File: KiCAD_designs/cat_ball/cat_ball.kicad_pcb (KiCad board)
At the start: 2 copper layers, 35 x 34.7 mm, 35 parts, among them J1 B2B-PH-SM4-TBLFSN, J2 B2B-PH-SM4-TBLFSN, U1 ATMEGA328P-AU, U2 MX1508

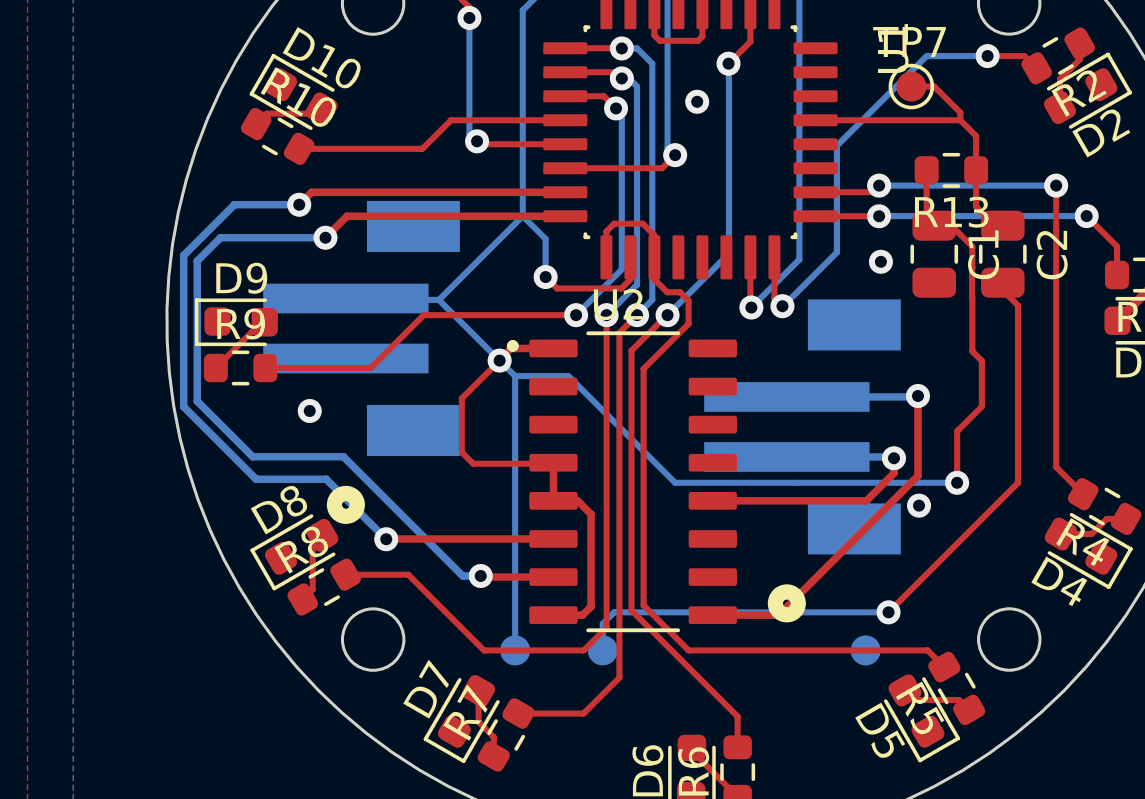
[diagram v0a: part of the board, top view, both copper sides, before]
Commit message: changed cat ball via size
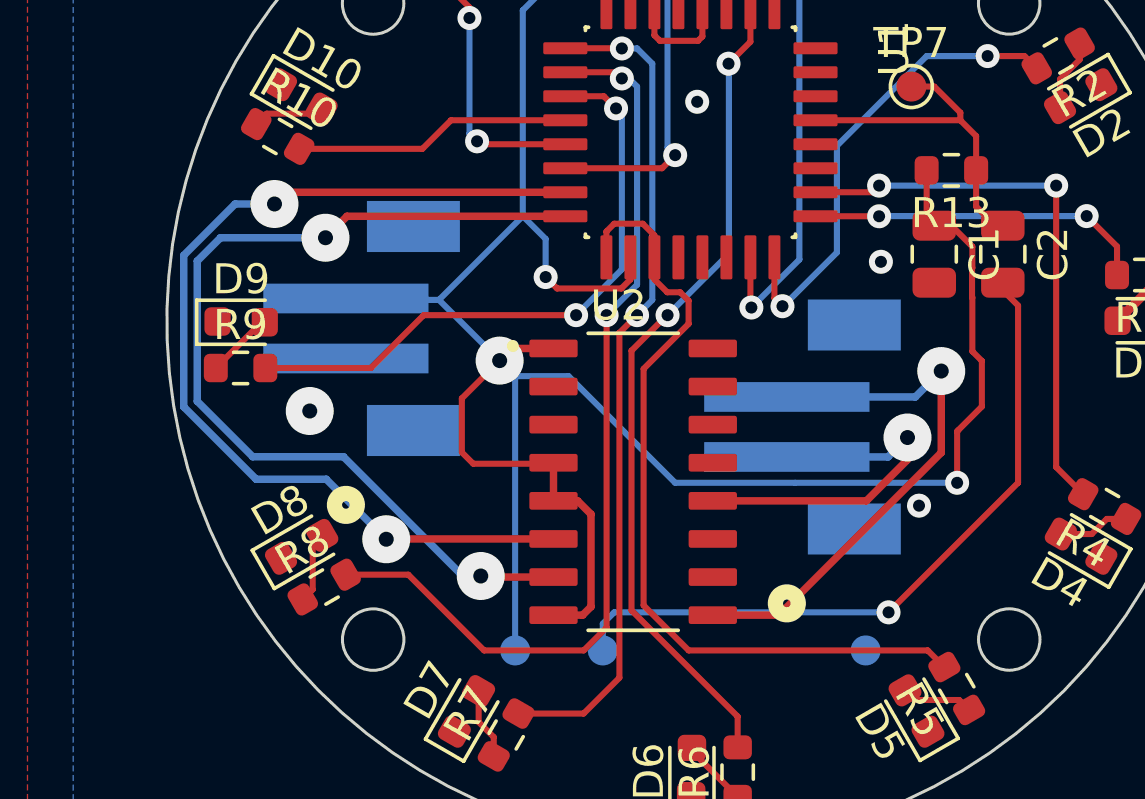
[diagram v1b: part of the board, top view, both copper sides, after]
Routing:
- net Net-(U2A-OUTB2): track 15.8 -> 18.1 mm
- net Net-(U2A-OUTA2): track 10.5 -> 12.1 mm
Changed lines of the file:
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@@
   (via (at 136.8 63.796) (size 0.8) (drill 0.4) (layers "F.Cu" "B.Cu") (net 1))
   (via (at 149.754 81.068) (size 0.8) (drill 0.4) (layers "F.Cu" "B.Cu") (net 1))
-  (via (at 134.505 76.995) (size 0.8) (drill 0.4) (layers "F.Cu" "B.Cu") (net 1))
+  (via (at 134.505 76.995) (size 1.6) (drill 0.5) (layers "F.Cu" "B.Cu") (net 1))
   (via (at 136.038 74.21) (size 0.8) (drill 0.4) (layers "F.Cu" "B.Cu") (net 1))
   (segment (start 136.038 74.21) (end 136.038 72.94) (width 0.2032) (layer "B.Cu") (net 1))
@@
   (via (at 147.214 73.702) (size 0.8) (drill 0.4) (layers "F.Cu" "B.Cu") (free) (net 2))
   (via (at 141.0896 68.368) (size 0.8) (drill 0.4) (layers "F.Cu" "B.Cu") (free) (net 2))
-  (via (at 128.175 78.675) (size 0.8) (drill 0.4) (layers "F.Cu" "B.Cu") (free) (net 2))
+  (via (at 128.175 78.675) (size 1.6) (drill 0.5) (layers "F.Cu" "B.Cu") (free) (net 2))
   (segment (start 150.388 70.654) (end 150.388 71.862) (width 0.2032) (layer "F.Cu") (net 3))
   (segment (start 145.034 68.984) (end 149.862 68.984) (width 0.2032) (layer "F.Cu") (net 3))
@@
   (segment (start 140.102 69.892) (end 140.102 63.796) (width 0.2032) (layer "B.Cu") (net 28))
   (segment (start 140.356 70.146) (end 140.102 69.892) (width 0.2032) (layer "B.Cu") (net 28))
-  (segment (start 136.694 71.384) (end 128.241 71.384) (width 0.25) (layer "F.Cu") (net 35))
+  (segment (start 127 71.775) (end 127.391 71.384) (width 0.25) (layer "F.Cu") (net 35))
   (segment (start 136.3 82.94) (end 130.735 82.94) (width 0.25) (layer "F.Cu") (net 35))
-  (segment (start 128.241 71.384) (end 127.825 71.8) (width 0.25) (layer "F.Cu") (net 35))
   (segment (start 130.735 82.94) (end 130.725 82.95) (width 0.25) (layer "F.Cu") (net 35))
-  (via (at 127.825 71.8) (size 0.8) (drill 0.4) (layers "F.Cu" "B.Cu") (net 35))
-  (via (at 130.725 82.95) (size 0.8) (drill 0.4) (layers "F.Cu" "B.Cu") (net 35))
-  (segment (start 130.725 82.95) (end 128.725 80.95) (width 0.25) (layer "B.Cu") (net 35))
-  (segment (start 125.663604 71.8) (end 127.825 71.8) (width 0.25) (layer "B.Cu") (net 35))
-  (segment (start 123.975 78.536396) (end 123.975 73.488604) (width 0.25) (layer "B.Cu") (net 35))
-  (segment (start 128.725 80.95) (end 126.388604 80.95) (width 0.25) (layer "B.Cu") (net 35))
-  (segment (start 126.388604 80.95) (end 123.975 78.536396) (width 0.25) (layer "B.Cu") (net 35))
-  (segment (start 123.975 73.488604) (end 125.663604 71.8) (width 0.25) (layer "B.Cu") (net 35))
+  (segment (start 127.391 71.384) (end 136.694 71.384) (width 0.25) (layer "F.Cu") (net 35))
+  (via (at 127 71.775) (size 1.6) (drill 0.5) (layers "F.Cu" "B.Cu") (net 35))
+  (via (at 130.725 82.95) (size 1.6) (drill 0.5) (layers "F.Cu" "B.Cu") (net 35))
+  (segment (start 123.975 73.488604) (end 123.975 78.536396) (width 0.25) (layer "B.Cu") (net 35))
+  (segment (start 123.975 78.536396) (end 126.388604 80.95) (width 0.25) (layer "B.Cu") (net 35))
+  (segment (start 126.388604 80.95) (end 128.725 80.95) (width 0.25) (layer "B.Cu") (net 35))
+  (segment (start 128.725 80.95) (end 130.725 82.95) (width 0.25) (layer "B.Cu") (net 35))
+  (segment (start 125.688604 71.775) (end 123.975 73.488604) (width 0.25) (layer "B.Cu") (net 35))
+  (segment (start 127 71.775) (end 125.688604 71.775) (width 0.25) (layer "B.Cu") (net 35))
   (segment (start 136.694 72.184) (end 129.416 72.184) (width 0.25) (layer "F.Cu") (net 36))
   (segment (start 129.416 72.184) (end 128.7 72.9) (width 0.25) (layer "F.Cu") (net 36))
   (segment (start 133.91 84.21) (end 133.875 84.175) (width 0.25) (layer "F.Cu") (net 36))
   (segment (start 136.3 84.21) (end 133.91 84.21) (width 0.25) (layer "F.Cu") (net 36))
-  (via (at 128.7 72.9) (size 0.8) (drill 0.4) (layers "F.Cu" "B.Cu") (net 36))
-  (via (at 133.875 84.175) (size 0.8) (drill 0.4) (layers "F.Cu" "B.Cu") (net 36))
+  (via (at 128.7 72.9) (size 1.6) (drill 0.5) (layers "F.Cu" "B.Cu") (net 36))
+  (via (at 133.875 84.175) (size 1.6) (drill 0.5) (layers "F.Cu" "B.Cu") (net 36))
   (segment (start 124.425 78.35) (end 124.425 73.675) (width 0.25) (layer "B.Cu") (net 36))
   (segment (start 126.275 80.2) (end 124.425 78.35) (width 0.25) (layer "B.Cu") (net 36))
@@
   (segment (start 124.425 73.675) (end 125.2 72.9) (width 0.25) (layer "B.Cu") (net 36))
   (segment (start 133.875 84.175) (end 133.275 84.175) (width 0.25) (layer "B.Cu") (net 36))
-  (segment (start 141.61 81.67) (end 146.73 81.67) (width 0.25) (layer "F.Cu") (net 41))
-  (segment (start 146.73 81.67) (end 147.65 80.75) (width 0.25) (layer "F.Cu") (net 41))
-  (segment (start 147.65 80.75) (end 147.65 80.25) (width 0.25) (layer "F.Cu") (net 41))
-  (via (at 147.65 80.25) (size 0.8) (drill 0.4) (layers "F.Cu" "B.Cu") (net 41))
-  (segment (start 147.60725 80.20725) (end 144.077949 80.20725) (width 0.25) (layer "B.Cu") (net 41))
-  (segment (start 147.65 80.25) (end 147.60725 80.20725) (width 0.25) (layer "B.Cu") (net 41))
+  (segment (start 148.1 80.3) (end 146.73 81.67) (width 0.25) (layer "F.Cu") (net 41))
+  (segment (start 146.73 81.67) (end 141.61 81.67) (width 0.25) (layer "F.Cu") (net 41))
+  (segment (start 148.1 79.558852) (end 148.1 80.3) (width 0.25) (layer "F.Cu") (net 41))
+  (via (at 148.1 79.558852) (size 1.6) (drill 0.5) (layers "F.Cu" "B.Cu") (net 41))
+  (segment (start 147.451602 80.20725) (end 144.077949 80.20725) (width 0.25) (layer "B.Cu") (net 41))
+  (segment (start 148.1 79.558852) (end 147.451602 80.20725) (width 0.25) (layer "B.Cu") (net 41))
+  (segment (start 149.225 77.343) (end 149.225 80.063695) (width 0.25) (layer "F.Cu") (net 42))
+  (segment (start 149.225 80.063695) (end 143.808695 85.48) (width 0.25) (layer "F.Cu") (net 42))
   (segment (start 143.808695 85.48) (end 141.61 85.48) (width 0.25) (layer "F.Cu") (net 42))
-  (segment (start 148.45 78.175) (end 148.45 80.838695) (width 0.25) (layer "F.Cu") (net 42))
-  (segment (start 148.45 80.838695) (end 143.808695 85.48) (width 0.25) (layer "F.Cu") (net 42))
-  (via (at 148.45 78.175) (size 0.8) (drill 0.4) (layers "F.Cu" "B.Cu") (net 42))
-  (segment (start 148.417752 78.207248) (end 148.45 78.175) (width 0.25) (layer "B.Cu") (net 42))
-  (segment (start 144.077949 78.207248) (end 148.417752 78.207248) (width 0.25) (layer "B.Cu") (net 42))
+  (via (at 149.225 77.343) (size 1.6) (drill 0.5) (layers "F.Cu" "B.Cu") (net 42))
+  (segment (start 149.225 77.343) (end 148.360752 78.207248) (width 0.25) (layer "B.Cu") (net 42))
+  (segment (start 148.360752 78.207248) (end 144.077949 78.207248) (width 0.25) (layer "B.Cu") (net 42))
   (zone (net 2) (net_name "GND") (layer "F.Cu") (hatch edge 0.5)
     (connect_pads (clearance 0.2))

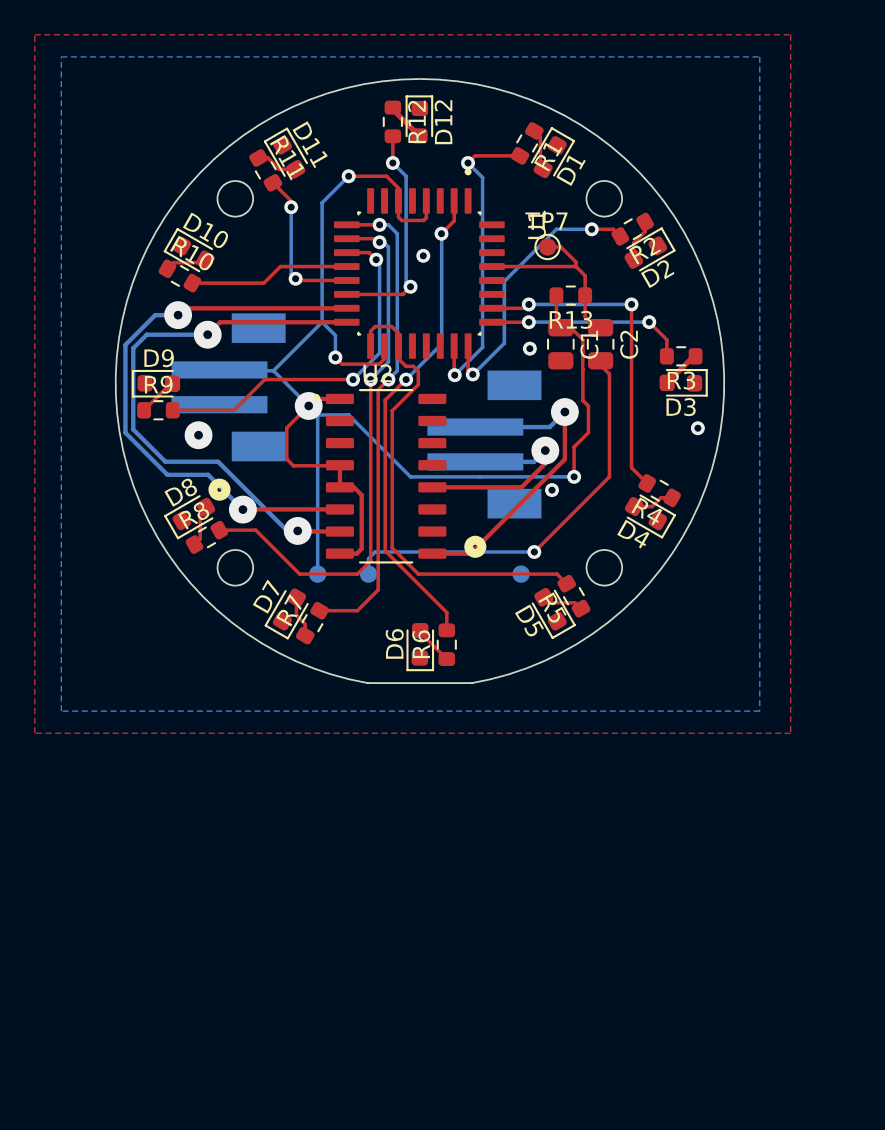
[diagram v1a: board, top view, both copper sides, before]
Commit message: catball thicker traces
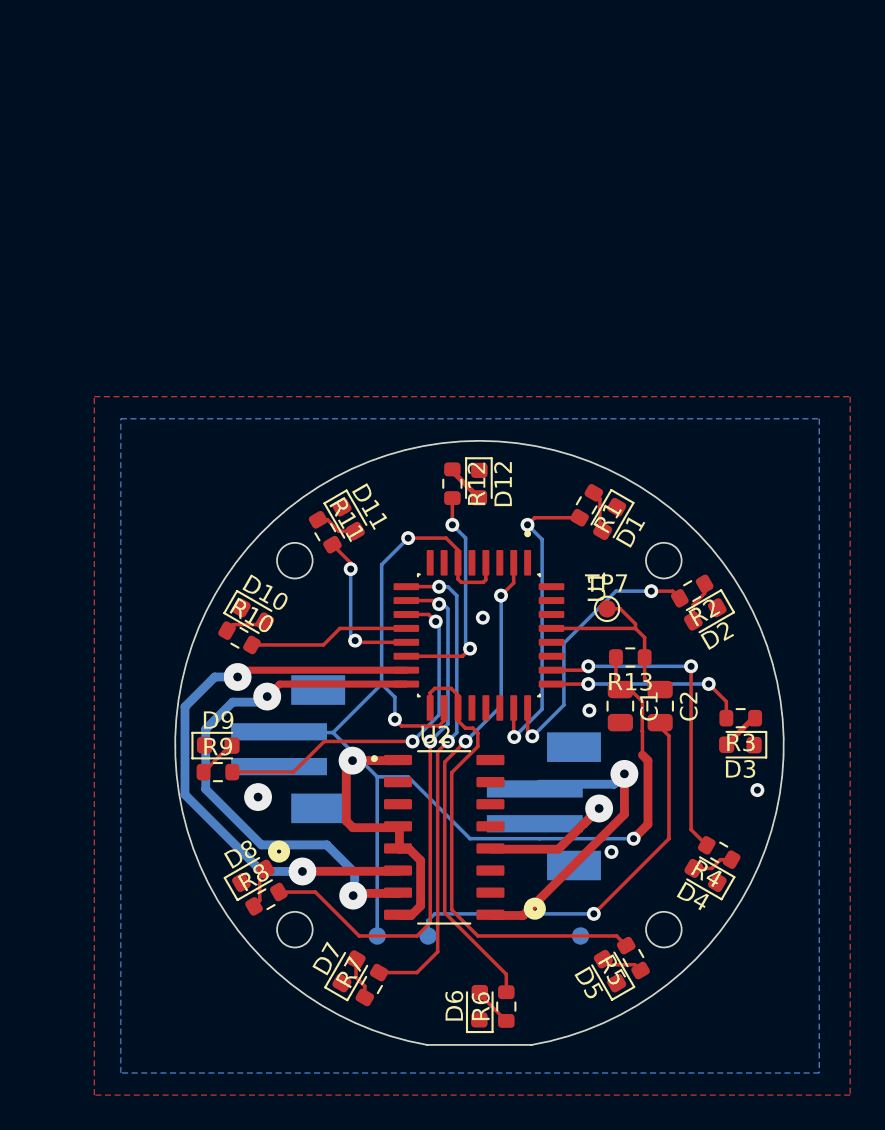
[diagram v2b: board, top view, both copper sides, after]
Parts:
- J1, J2: footprint esp_lib:B2B-PH-SM4-TBLFSN_JST -> IO_watch_cat_ball:B2B-PH-SM4-TBLFSN_JST
- U2: footprint esp_lib:MX1508 -> IO_watch_cat_ball:MX1508
- moved C1 21.1 mm to (152.4, 94.2)
- moved C2 21.1 mm to (154.7, 94.2)
- moved D3 21.1 mm to (159.3, 96.5)
- moved D5 21.1 mm to (151.8, 109.5)
- moved D7 21.1 mm to (136.8, 109.5)
- moved D9 21.1 mm to (129.3, 96.5)
- moved R13 21.1 mm to (153.0, 91.4)
- moved R2 21.1 mm to (156.5, 87.6)
- moved R6 21.1 mm to (145.9, 111.5)
- moved R7 21.1 mm to (138.1, 110.3)
- moved TP7 21.1 mm to (151.6, 88.7)
- moved D1 21.1 mm to (151.8, 83.5)
- moved D11 21.1 mm to (136.8, 83.5)
- moved D2 21.1 mm to (157.3, 89.0)
- moved D4 21.1 mm to (157.3, 104.0)
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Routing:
- net Net-(U2A-OUTA2): track 12.1 -> 11.2 mm
- net /D12: track 31.9 -> 31.1 mm
- net VCC: track 89.2 -> 89.9 mm
